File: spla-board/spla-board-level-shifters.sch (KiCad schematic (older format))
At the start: 0 parts

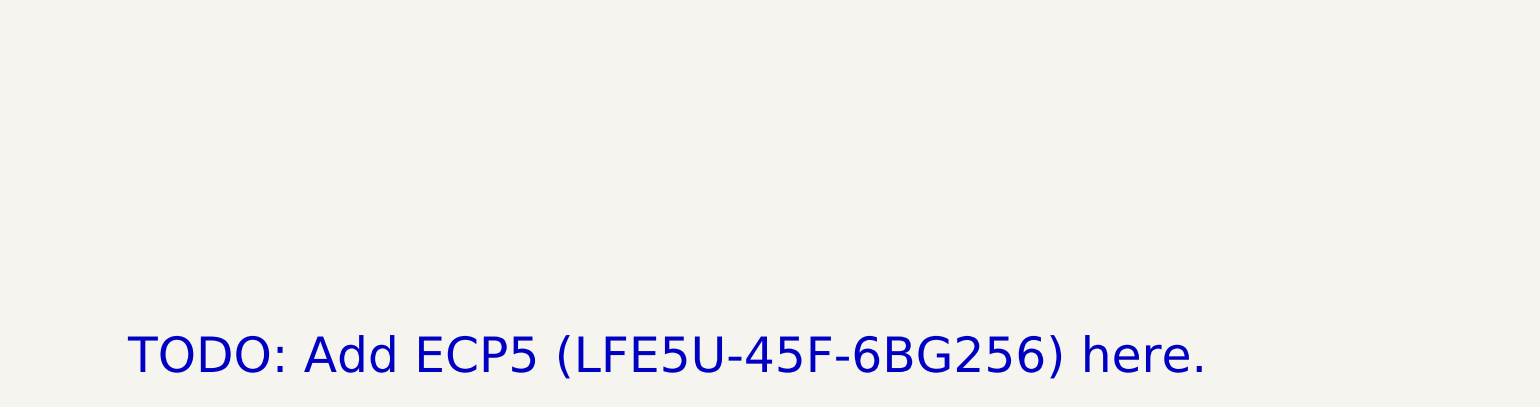
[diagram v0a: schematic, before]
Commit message: schematic: Add blank sheets for future components; rearrange root sheet.
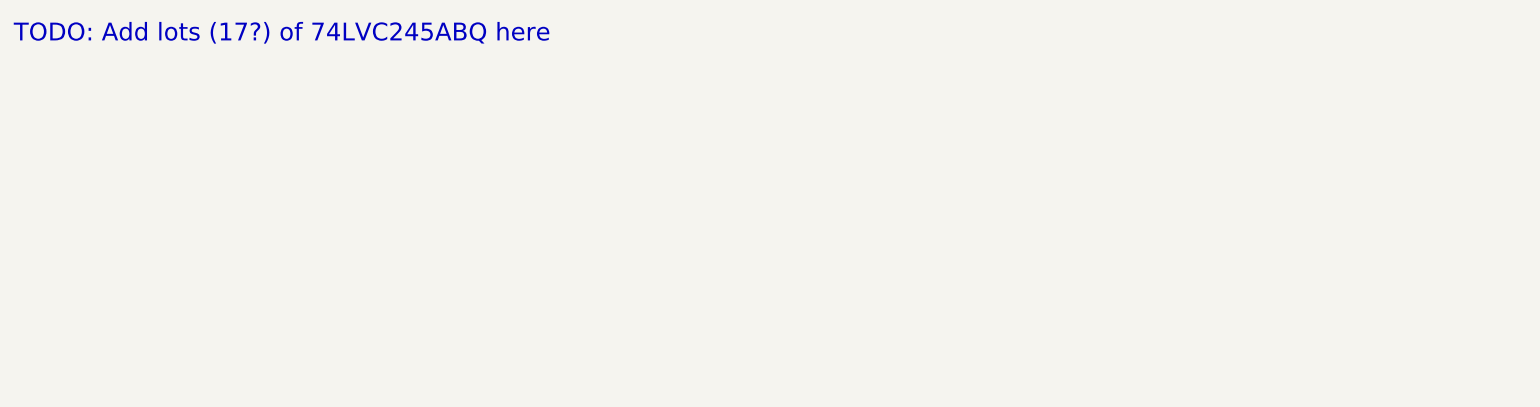
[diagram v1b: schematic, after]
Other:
- note added: "TODO: Add lots (17?) of 74LVC245ABQ here"
- note removed: "TODO: Add ECP5 (LFE5U-45F-6BG256) here."
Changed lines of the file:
@@
 EELAYER 30 0
 EELAYER END
-$Descr A3 16535 11693
+$Descr A4 11693 8268
 encoding utf-8
-Sheet 3 8
-Title "SPLA Board - FPGA"
+Sheet 8 8
+Title ""
 Date "2020-02-21"
 Rev "3"
@@
 Comment4 ""
 $EndDescr
-Text Notes 4900 5650 0    202  ~ 0
-TODO: Add ECP5 (LFE5U-45F-6BG256) here.
+Text Notes 4250 3750 0    101  ~ 0
+TODO: Add lots (17?) of 74LVC245ABQ here
 $EndSCHEMATC

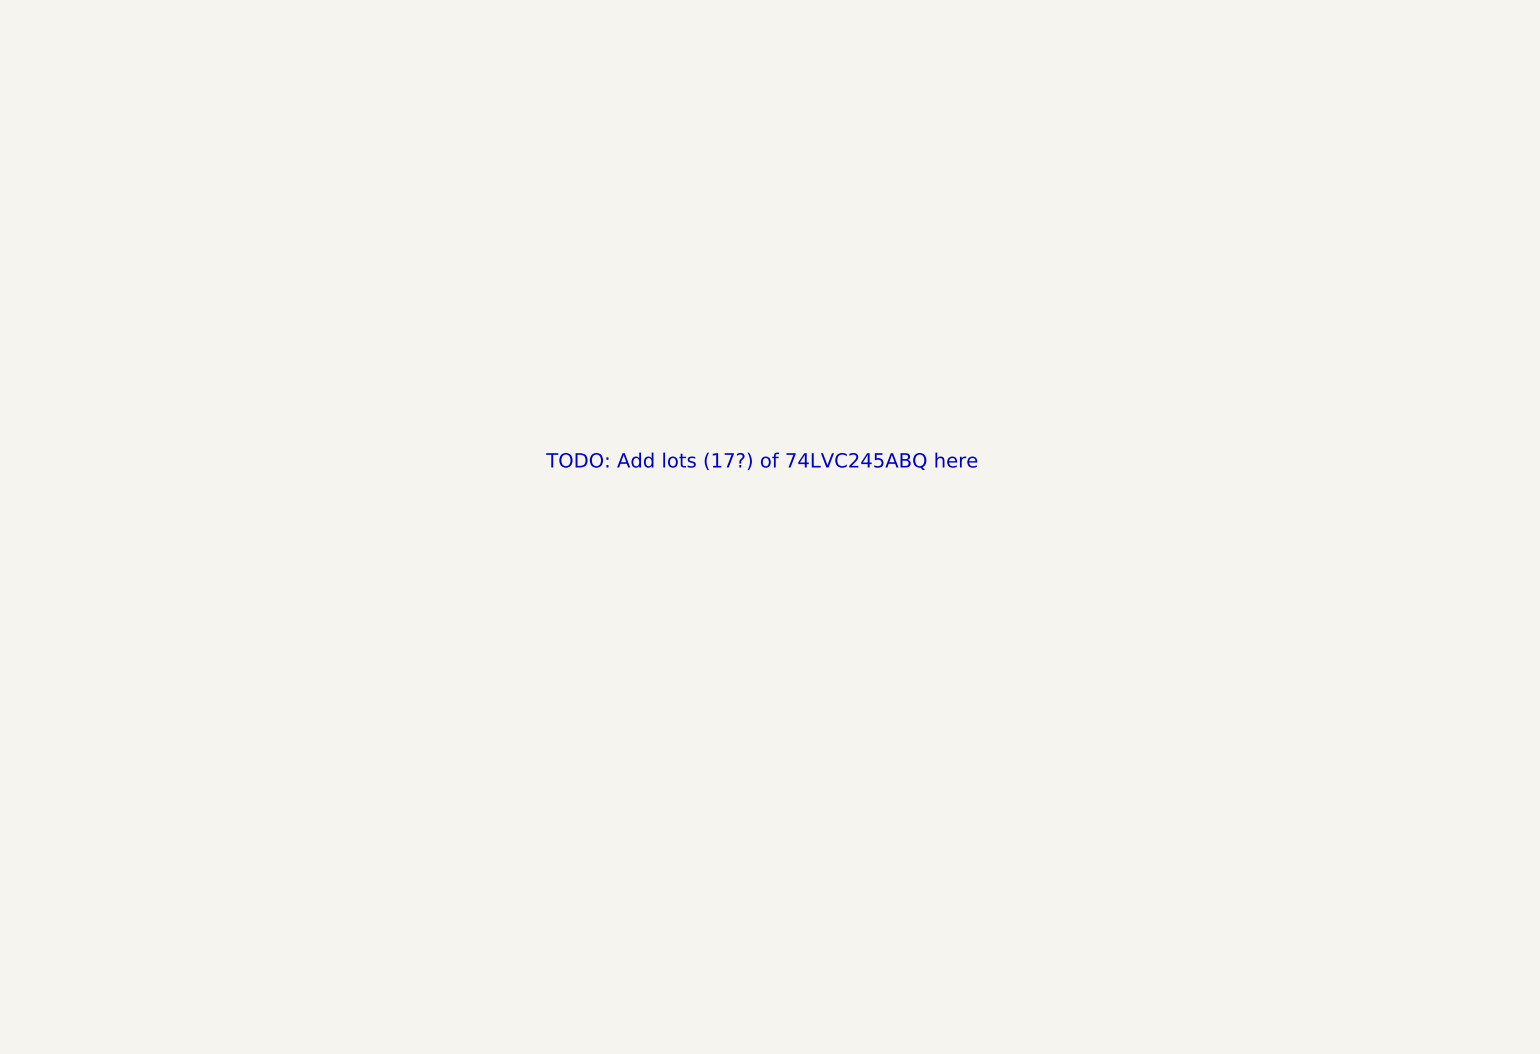
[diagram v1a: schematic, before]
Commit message: schematic: Add level shifters and PPU reset jumpers.
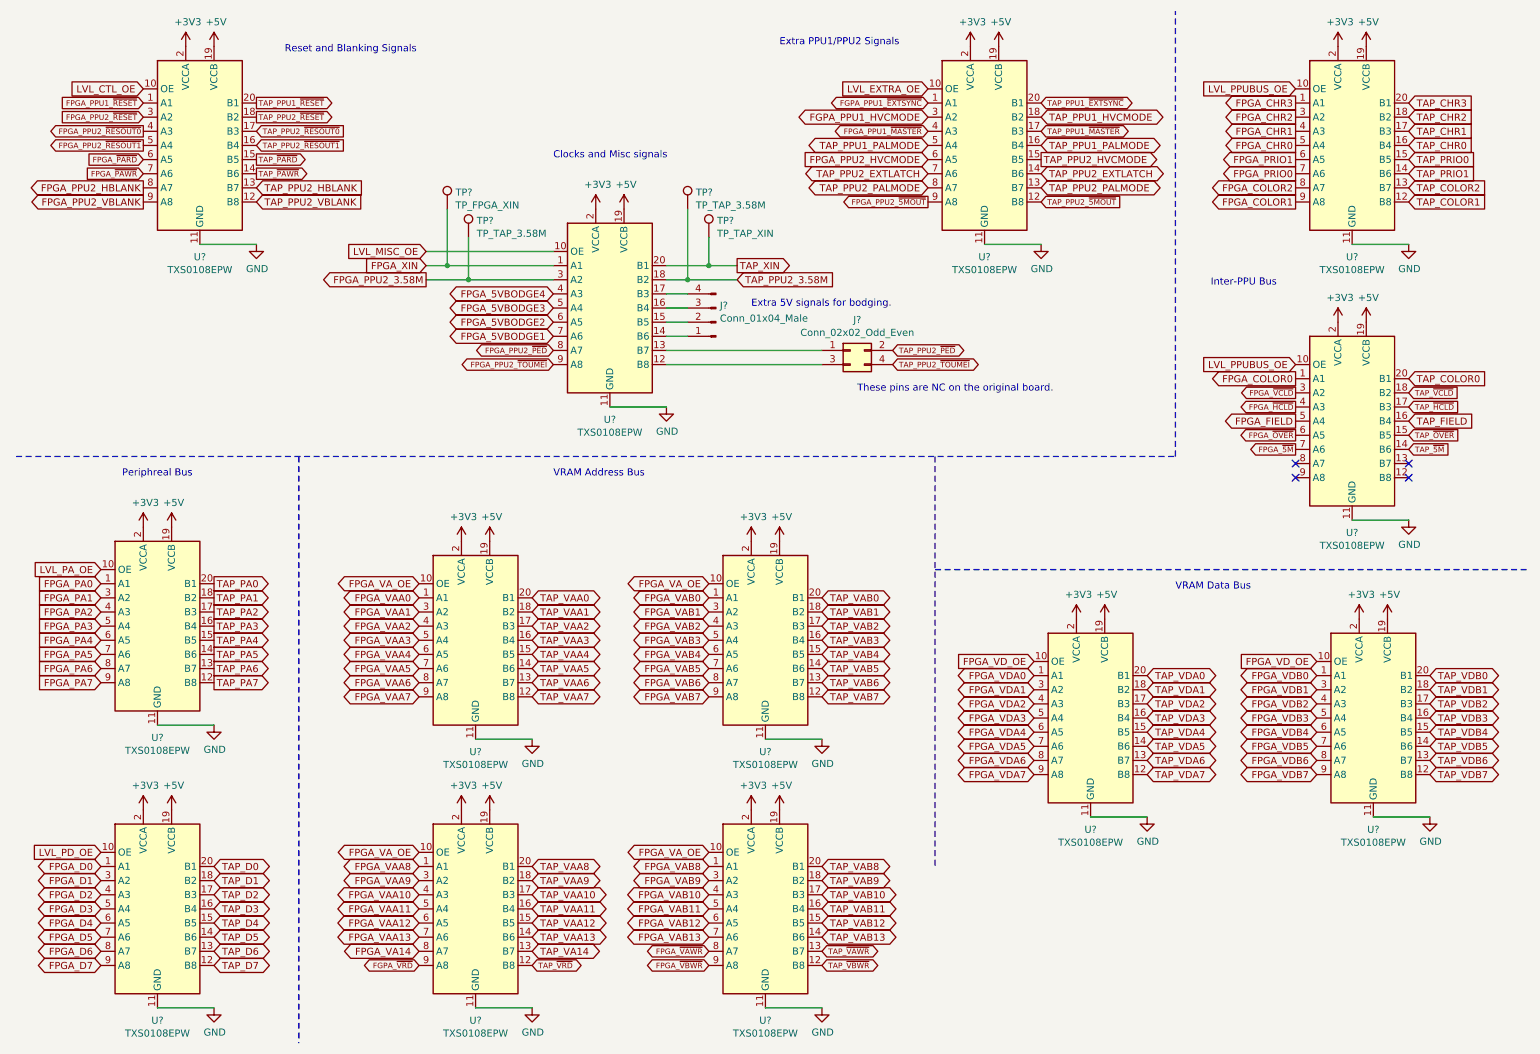
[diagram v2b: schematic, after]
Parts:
- added J?: Conn_02x02_Odd_Even, symbol Connector_Generic:Conn_02x02_Odd_Even
- added J?: Conn_01x04_Male, symbol Connector:Conn_01x04_Male
- added TP?: TP_FPGA_XIN, symbol Connector:TestPoint
- added TP?: TP_TAP_XIN, symbol Connector:TestPoint
- added TP? (x2): TP_TAP_3.58M, symbol Connector:TestPoint
- added U? (x13): TXS0108EPW, Package_SO:TSSOP-20_4.4x6.5mm_P0.65mm, symbol Logic_LevelTranslator:TXS0108EPW
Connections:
- new net: J?.1 (Pin_1), U?.13 (B7)
- new net: J?.3 (Pin_3), U?.12 (B8)
- new net: J?.1 (Pin_1), U?.14 (B6)
- new net: J?.2 (Pin_2), U?.15 (B5)
- new net: J?.3 (Pin_3), U?.16 (B4)
- new net: J?.4 (Pin_4), U?.17 (B3)
- new net +3V3: U?.2 (VCCA), U?.2 (VCCA), U?.2 (VCCA), U?.2 (VCCA), U?.2 (VCCA), U?.2 (VCCA), U?.2 (VCCA), U?.2 (VCCA), U?.2 (VCCA), U?.2 (VCCA), U?.2 (VCCA), U?.2 (VCCA), U?.2 (VCCA)
- new net +5V: U?.19 (VCCB), U?.19 (VCCB), U?.19 (VCCB), U?.19 (VCCB), U?.19 (VCCB), U?.19 (VCCB), U?.19 (VCCB), U?.19 (VCCB), U?.19 (VCCB), U?.19 (VCCB), U?.19 (VCCB), U?.19 (VCCB), U?.19 (VCCB)
- new net FGPA_PPU1_HVCMODE: U?.3 (A2)
- new net FGPA_PPU1_~EXTSYNC~: U?.1 (A1)
- new net FGPA_~VRD~: U?.9 (A8)
- new net FPGA_5VBODGE1: U?.7 (A6)
- new net FPGA_5VBODGE2: U?.6 (A5)
- new net FPGA_5VBODGE3: U?.5 (A4)
- new net FPGA_5VBODGE4: U?.4 (A3)
- new net FPGA_CHR0: U?.5 (A4)
- new net FPGA_CHR1: U?.4 (A3)
- new net FPGA_CHR2: U?.3 (A2)
- new net FPGA_CHR3: U?.1 (A1)
- new net FPGA_COLOR0: U?.1 (A1)
- new net FPGA_COLOR1: U?.9 (A8)
- new net FPGA_COLOR2: U?.8 (A7)
- new net FPGA_D0: U?.1 (A1)
- new net FPGA_D1: U?.3 (A2)
- new net FPGA_D2: U?.4 (A3)
- new net FPGA_D3: U?.5 (A4)
- new net FPGA_D4: U?.6 (A5)
- new net FPGA_D5: U?.7 (A6)
- new net FPGA_D6: U?.8 (A7)
- new net FPGA_D7: U?.9 (A8)
- new net FPGA_FIELD: U?.5 (A4)
- new net FPGA_PA0: U?.1 (A1)
- new net FPGA_PA1: U?.3 (A2)
- new net FPGA_PA2: U?.4 (A3)
- new net FPGA_PA3: U?.5 (A4)
- new net FPGA_PA4: U?.6 (A5)
- new net FPGA_PA5: U?.7 (A6)
- new net FPGA_PA6: U?.8 (A7)
- new net FPGA_PA7: U?.9 (A8)
- new net FPGA_PPU1_~MASTER~: U?.4 (A3)
- new net FPGA_PPU1_~RESET~: U?.1 (A1)
- new net FPGA_PPU2_3.58M: TP?.1, U?.3 (A2)
- new net FPGA_PPU2_HBLANK: U?.8 (A7)
- new net FPGA_PPU2_HVCMODE: U?.6 (A5)
- new net FPGA_PPU2_VBLANK: U?.9 (A8)
- new net FPGA_PPU2_~5MOUT~: U?.9 (A8)
- new net FPGA_PPU2_~PED~: U?.8 (A7)
- new net FPGA_PPU2_~RESET~: U?.3 (A2)
- new net FPGA_PPU2_~RESOUT0~: U?.4 (A3)
- new net FPGA_PPU2_~RESOUT1~: U?.5 (A4)
- new net FPGA_PPU2_~TOUMEI~: U?.9 (A8)
- new net FPGA_PRIO0: U?.7 (A6)
- new net FPGA_PRIO1: U?.6 (A5)
- new net FPGA_VA14: U?.8 (A7)
- new net FPGA_VAA0: U?.1 (A1)
- new net FPGA_VAA1: U?.3 (A2)
- new net FPGA_VAA10: U?.4 (A3)
- new net FPGA_VAA11: U?.5 (A4)
- new net FPGA_VAA12: U?.6 (A5)
- new net FPGA_VAA13: U?.7 (A6)
- new net FPGA_VAA2: U?.4 (A3)
- new net FPGA_VAA3: U?.5 (A4)
- new net FPGA_VAA4: U?.6 (A5)
- new net FPGA_VAA5: U?.7 (A6)
- new net FPGA_VAA6: U?.8 (A7)
- new net FPGA_VAA7: U?.9 (A8)
- new net FPGA_VAA8: U?.1 (A1)
- new net FPGA_VAA9: U?.3 (A2)
- new net FPGA_VAB0: U?.1 (A1)
- new net FPGA_VAB1: U?.3 (A2)
- new net FPGA_VAB10: U?.4 (A3)
- new net FPGA_VAB11: U?.5 (A4)
- new net FPGA_VAB12: U?.6 (A5)
- new net FPGA_VAB13: U?.7 (A6)
- new net FPGA_VAB2: U?.4 (A3)
- new net FPGA_VAB3: U?.5 (A4)
- new net FPGA_VAB4: U?.6 (A5)
- new net FPGA_VAB5: U?.7 (A6)
- new net FPGA_VAB6: U?.8 (A7)
- new net FPGA_VAB7: U?.9 (A8)
- new net FPGA_VAB8: U?.1 (A1)
- new net FPGA_VAB9: U?.3 (A2)
- new net FPGA_VA_OE: U?.10 (OE), U?.10 (OE), U?.10 (OE), U?.10 (OE)
- new net FPGA_VDA0: U?.1 (A1)
- new net FPGA_VDA1: U?.3 (A2)
- new net FPGA_VDA2: U?.4 (A3)
- new net FPGA_VDA3: U?.5 (A4)
- new net FPGA_VDA4: U?.6 (A5)
- new net FPGA_VDA5: U?.7 (A6)
- new net FPGA_VDA6: U?.8 (A7)
- new net FPGA_VDA7: U?.9 (A8)
- new net FPGA_VDB0: U?.1 (A1)
- new net FPGA_VDB1: U?.3 (A2)
- new net FPGA_VDB2: U?.4 (A3)
- new net FPGA_VDB3: U?.5 (A4)
- new net FPGA_VDB4: U?.6 (A5)
- new net FPGA_VDB5: U?.7 (A6)
- new net FPGA_VDB6: U?.8 (A7)
- new net FPGA_VDB7: U?.9 (A8)
- new net FPGA_VD_OE: U?.10 (OE), U?.10 (OE)
- new net FPGA_XIN: TP?.1, U?.1 (A1)
- new net FPGA_~5M~: U?.7 (A6)
- new net FPGA_~HCLD: U?.4 (A3)
- new net FPGA_~OVER~: U?.6 (A5)
- new net FPGA_~PARD~: U?.6 (A5)
- new net FPGA_~PAWR~: U?.7 (A6)
- new net FPGA_~VAWR~: U?.8 (A7)
- new net FPGA_~VBWR~: U?.9 (A8)
- new net FPGA_~VCLD~: U?.3 (A2)
- new net GND: U?.11 (GND), U?.11 (GND), U?.11 (GND), U?.11 (GND), U?.11 (GND), U?.11 (GND), U?.11 (GND), U?.11 (GND), U?.11 (GND), U?.11 (GND), U?.11 (GND), U?.11 (GND), U?.11 (GND)
- new net LVL_CTL_OE: U?.10 (OE)
- new net LVL_EXTRA_OE: U?.10 (OE)
- new net LVL_MISC_OE: U?.10 (OE)
- new net LVL_PA_OE: U?.10 (OE)
- new net LVL_PD_OE: U?.10 (OE)
- new net LVL_PPUBUS_OE: U?.10 (OE), U?.10 (OE)
- new net TAP_CHR0: U?.16 (B4)
- new net TAP_CHR1: U?.17 (B3)
- new net TAP_CHR2: U?.18 (B2)
- new net TAP_CHR3: U?.20 (B1)
- new net TAP_COLOR0: U?.20 (B1)
- new net TAP_COLOR1: U?.12 (B8)
- new net TAP_COLOR2: U?.13 (B7)
- new net TAP_D0: U?.20 (B1)
- new net TAP_D1: U?.18 (B2)
- new net TAP_D2: U?.17 (B3)
- new net TAP_D3: U?.16 (B4)
- new net TAP_D4: U?.15 (B5)
- new net TAP_D5: U?.14 (B6)
- new net TAP_D6: U?.13 (B7)
- new net TAP_D7: U?.12 (B8)
- new net TAP_FIELD: U?.16 (B4)
- new net TAP_PA0: U?.20 (B1)
- new net TAP_PA1: U?.18 (B2)
- new net TAP_PA2: U?.17 (B3)
- new net TAP_PA3: U?.16 (B4)
- new net TAP_PA4: U?.15 (B5)
- new net TAP_PA5: U?.14 (B6)
- new net TAP_PA6: U?.13 (B7)
- new net TAP_PA7: U?.12 (B8)
- new net TAP_PPU1_HVCMODE: U?.18 (B2)
- new net TAP_PPU1_PALMODE: U?.16 (B4), U?.5 (A4)
- new net TAP_PPU1_~EXTSYNC~: U?.20 (B1)
- new net TAP_PPU1_~MASTER~: U?.17 (B3)
- new net TAP_PPU1_~RESET~: U?.20 (B1)
- new net TAP_PPU2_3.58M: TP?.1, U?.18 (B2)
- new net TAP_PPU2_EXTLATCH: U?.14 (B6), U?.7 (A6)
- new net TAP_PPU2_HBLANK: U?.13 (B7)
- new net TAP_PPU2_HVCMODE: U?.15 (B5)
- new net TAP_PPU2_PALMODE: U?.13 (B7), U?.8 (A7)
- new net TAP_PPU2_VBLANK: U?.12 (B8)
- new net TAP_PPU2_~5MOUT~: U?.12 (B8)
- new net TAP_PPU2_~PED~: J?.2 (Pin_2)
- new net TAP_PPU2_~RESET~: U?.18 (B2)
- new net TAP_PPU2_~RESOUT0~: U?.17 (B3)
- new net TAP_PPU2_~RESOUT1~: U?.16 (B4)
- new net TAP_PPU2_~TOUMEI~: J?.4 (Pin_4)
- new net TAP_PRIO0: U?.15 (B5)
- new net TAP_PRIO1: U?.14 (B6)
- new net TAP_VA14: U?.13 (B7)
- new net TAP_VAA0: U?.20 (B1)
- new net TAP_VAA1: U?.18 (B2)
- new net TAP_VAA10: U?.17 (B3)
- new net TAP_VAA11: U?.16 (B4)
- new net TAP_VAA12: U?.15 (B5)
- new net TAP_VAA13: U?.14 (B6)
- new net TAP_VAA2: U?.17 (B3)
- new net TAP_VAA3: U?.16 (B4)
- new net TAP_VAA4: U?.15 (B5)
- new net TAP_VAA5: U?.14 (B6)
- new net TAP_VAA6: U?.13 (B7)
- new net TAP_VAA7: U?.12 (B8)
- new net TAP_VAA8: U?.20 (B1)
- new net TAP_VAA9: U?.18 (B2)
- new net TAP_VAB0: U?.20 (B1)
- new net TAP_VAB1: U?.18 (B2)
- new net TAP_VAB10: U?.17 (B3)
- new net TAP_VAB11: U?.16 (B4)
- new net TAP_VAB12: U?.15 (B5)
- new net TAP_VAB13: U?.14 (B6)
- new net TAP_VAB2: U?.17 (B3)
- new net TAP_VAB3: U?.16 (B4)
- new net TAP_VAB4: U?.15 (B5)
- new net TAP_VAB5: U?.14 (B6)
- new net TAP_VAB6: U?.13 (B7)
- new net TAP_VAB7: U?.12 (B8)
- new net TAP_VAB8: U?.20 (B1)
- new net TAP_VAB9: U?.18 (B2)
- new net TAP_VDA0: U?.20 (B1)
- new net TAP_VDA1: U?.18 (B2)
- new net TAP_VDA2: U?.17 (B3)
- new net TAP_VDA3: U?.16 (B4)
- new net TAP_VDA4: U?.15 (B5)
- new net TAP_VDA5: U?.14 (B6)
- new net TAP_VDA6: U?.13 (B7)
- new net TAP_VDA7: U?.12 (B8)
- new net TAP_VDB0: U?.20 (B1)
- new net TAP_VDB1: U?.18 (B2)
- new net TAP_VDB2: U?.17 (B3)
- new net TAP_VDB3: U?.16 (B4)
- new net TAP_VDB4: U?.15 (B5)
- new net TAP_VDB5: U?.14 (B6)
- new net TAP_VDB6: U?.13 (B7)
- new net TAP_VDB7: U?.12 (B8)
- new net TAP_XIN: TP?.1, U?.20 (B1)
- new net TAP_~5M~: U?.14 (B6)
- new net TAP_~HCLD~: U?.17 (B3)
- new net TAP_~OVER~: U?.15 (B5)
- new net TAP_~PARD~: U?.15 (B5)
- new net TAP_~PAWR~: U?.14 (B6)
- new net TAP_~VAWR~: U?.13 (B7)
- new net TAP_~VBWR~: U?.12 (B8)
- new net TAP_~VCLD~: U?.18 (B2)
- new net TAP_~VRD~: U?.12 (B8)
- no-connect marks 0 -> 4
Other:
- note added: "Clocks and Misc signals"
- note added: "Extra 5V signals for bodging."
- note added: "Extra PPU1/PPU2 Signals"
- note added: "Inter-PPU Bus\n"
- note added: "Periphreal Bus"
- note added: "Reset and Blanking Signals"
- note added: "These pins are NC on the original board."
- note added: "VRAM Address Bus"
- note added: "VRAM Data Bus"
- note removed: "TODO: Add lots (17?) of 74LVC245ABQ here"

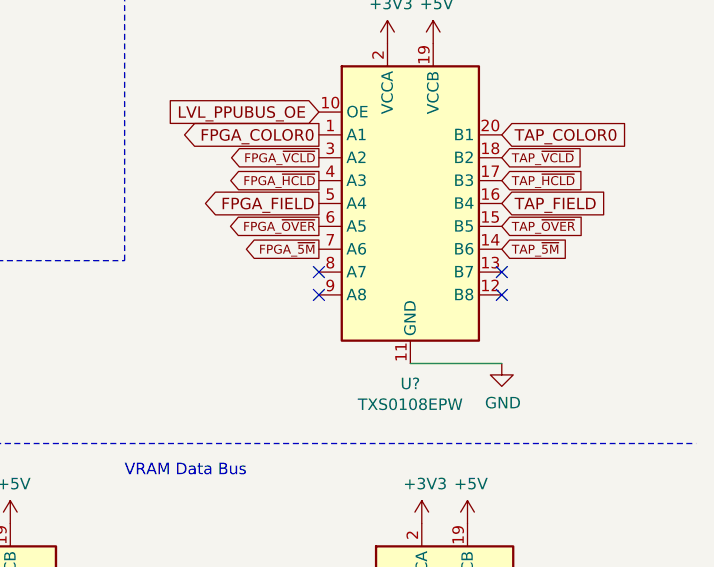
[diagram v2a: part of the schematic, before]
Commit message: reference: Add TXS0108E datasheet.
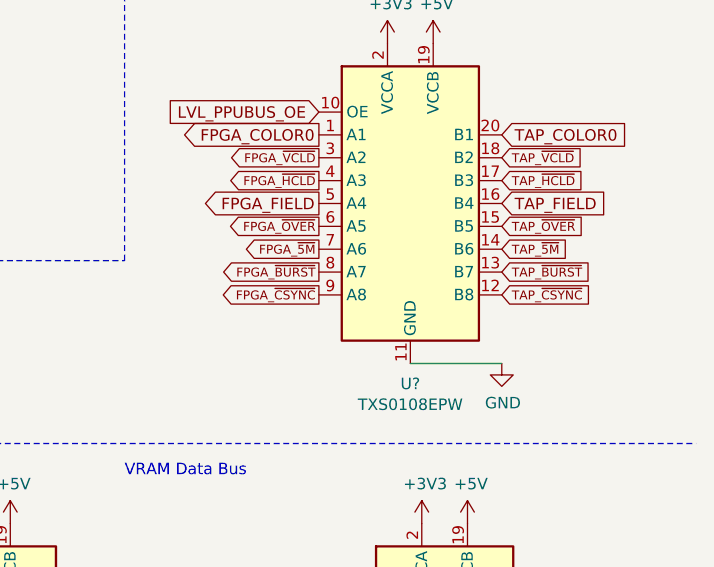
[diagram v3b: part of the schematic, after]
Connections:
- net TAP_~CSYNC~: now reaches U?.12 (B8)
- net TAP_~BURST~: now reaches U?.13 (B7)
- net FPGA_~BURST~: now reaches U?.8 (A7)
- net FPGA_~CSYNC~: now reaches U?.9 (A8)
- no-connect marks 4 -> 0
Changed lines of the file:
@@
 Wire Notes Line
 	500  3650 8700 3650
-NoConn ~ 9550 3700
-NoConn ~ 9550 3800
-NoConn ~ 10350 3800
-NoConn ~ 10350 3700
 $Comp
 L Logic_LevelTranslator:TXS0108EPW U?
@@
 Wire Wire Line
 	3400 2200 4300 2200
+Text GLabel 9550 3700 0    39   Output ~ 0
+FPGA_~BURST~
+Text GLabel 9550 3800 0    39   Output ~ 0
+FPGA_~CSYNC~
+Text GLabel 10350 3700 2    39   Input ~ 0
+TAP_~BURST~
+Text GLabel 10350 3800 2    39   Input ~ 0
+TAP_~CSYNC~
 $EndSCHEMATC
